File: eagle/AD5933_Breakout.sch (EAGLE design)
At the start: 6 parts, among them U1 AD5933

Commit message: first iteration of board
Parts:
- removed JP3: (no value), SparkFun-Connectors:M04PTH
- added JP1: (no value), SparkFun-Connectors:M04PTH
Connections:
- new net MCLK: JP1.3
- new net SCL: JP1.1
- new net SDA: JP1.2
- new net VCC: JP2.1
- net GND: now also JP1.4
- net RFB: now also JP2.3
- net VIN: now also JP2.2
- net VOUT: now also JP2.4
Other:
- moved on the sheet: JP2
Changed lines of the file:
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@@
 <part name="C2" library="SparkFun-Capacitors" deviceset="0.1UF-100V-10%(0603)" device="" value="10uF"/>
 <part name="GND2" library="SparkFun-Aesthetics" deviceset="GND" device=""/>
+<part name="JP1" library="SparkFun-Connectors" deviceset="M04" device="PTH"/>
 <part name="JP2" library="SparkFun-Connectors" deviceset="M04" device="PTH"/>
-<part name="JP3" library="SparkFun-Connectors" deviceset="M04" device="PTH"/>
 </parts>
 <sheets>
@@
 <instance part="C2" gate="G$1" x="213.36" y="109.22"/>
 <instance part="GND2" gate="1" x="157.48" y="93.98"/>
-<instance part="JP2" gate="G$1" x="93.98" y="96.52"/>
-<instance part="JP3" gate="G$1" x="99.06" y="121.92"/>
+<instance part="JP1" gate="G$1" x="91.44" y="96.52"/>
+<instance part="JP2" gate="G$1" x="96.52" y="121.92"/>
 </instances>
 <busses>
@@
 <wire x1="101.6" y1="93.98" x2="104.14" y2="93.98" width="0.1524" layer="91"/>
 <label x="101.6" y="93.98" size="1.778" layer="95"/>
+<pinref part="JP1" gate="G$1" pin="1"/>
 </segment>
 </net>
@@
 <wire x1="96.52" y1="96.52" x2="104.14" y2="96.52" width="0.1524" layer="91"/>
 <label x="101.6" y="96.52" size="1.778" layer="95"/>
+<pinref part="JP1" gate="G$1" pin="2"/>
 </segment>
 </net>
@@
 <wire x1="96.52" y1="99.06" x2="104.14" y2="99.06" width="0.1524" layer="91"/>
 <label x="101.6" y="99.06" size="1.778" layer="95"/>
+<pinref part="JP1" gate="G$1" pin="3"/>
 </segment>
 </net>
@@
 <wire x1="101.6" y1="121.92" x2="109.22" y2="121.92" width="0.1524" layer="91"/>
 <label x="106.68" y="121.92" size="1.778" layer="95"/>
+<pinref part="JP2" gate="G$1" pin="2"/>
 </segment>
 </net>
@@
 <wire x1="101.6" y1="124.46" x2="109.22" y2="124.46" width="0.1524" layer="91"/>
 <label x="106.68" y="124.46" size="1.778" layer="95"/>
+<pinref part="JP2" gate="G$1" pin="3"/>
 </segment>
 </net>
@@
 <wire x1="101.6" y1="127" x2="109.22" y2="127" width="0.1524" layer="91"/>
 <label x="106.68" y="127" size="1.778" layer="95"/>
+<pinref part="JP2" gate="G$1" pin="4"/>
 </segment>
 </net>
@@
 <wire x1="96.52" y1="101.6" x2="104.14" y2="101.6" width="0.1524" layer="91"/>
 <label x="101.6" y="101.6" size="1.778" layer="95"/>
+<pinref part="JP1" gate="G$1" pin="4"/>
 </segment>
 </net>
@@
 <wire x1="101.6" y1="119.38" x2="109.22" y2="119.38" width="0.1524" layer="91"/>
 <label x="106.68" y="119.38" size="1.778" layer="95"/>
+<pinref part="JP2" gate="G$1" pin="1"/>
 </segment>
 </net>

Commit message: both board and schematic looking good
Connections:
- removed net DVDD: C1.1, C2.1, U1.AVDD1, U1.AVDD2, U1.DVDD
- net MCLK: now also U1.MCLK
- net SCL: now also U1.SCL
- net SDA: now also U1.SDA
- net VCC: now also C1.1, C2.1, U1.AVDD1, U1.AVDD2, U1.DVDD
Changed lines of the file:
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@@
 <part name="FRAME1" library="SparkFun-Aesthetics" deviceset="FRAME-LETTER" device=""/>
 <part name="GND1" library="SparkFun-Aesthetics" deviceset="GND" device=""/>
-<part name="SUPPLY1" library="SparkFun-Aesthetics" deviceset="VCC" device=""/>
+<part name="VCC" library="SparkFun-Aesthetics" deviceset="VCC" device=""/>
 <part name="C1" library="SparkFun-Capacitors" deviceset="0.1UF-100V-10%(0603)" device="" value="0.1uF"/>
 <part name="C2" library="SparkFun-Capacitors" deviceset="0.1UF-100V-10%(0603)" device="" value="10uF"/>
@@
 <instance part="FRAME1" gate="G$2" x="193.04" y="2.54"/>
 <instance part="GND1" gate="1" x="213.36" y="99.06"/>
-<instance part="SUPPLY1" gate="1" x="213.36" y="124.46"/>
+<instance part="VCC" gate="1" x="213.36" y="124.46"/>
 <instance part="C1" gate="G$1" x="203.2" y="109.22"/>
 <instance part="C2" gate="G$1" x="213.36" y="109.22"/>
@@
 <net name="SCL" class="0">
 <segment>
-<wire x1="139.7" y1="124.46" x2="132.08" y2="124.46" width="0.1524" layer="91"/>
-<label x="127" y="124.46" size="1.778" layer="95"/>
-</segment>
-<segment>
 <wire x1="96.52" y1="93.98" x2="99.06" y2="93.98" width="0.1524" layer="91"/>
 <wire x1="99.06" y1="93.98" x2="101.6" y2="93.98" width="0.1524" layer="91"/>
@@
 <pinref part="JP1" gate="G$1" pin="1"/>
 </segment>
+<segment>
+<pinref part="U1" gate="A" pin="SCL"/>
+<wire x1="137.16" y1="124.46" x2="132.08" y2="124.46" width="0.1524" layer="91"/>
+<label x="127" y="124.46" size="1.778" layer="95"/>
+</segment>
 </net>
 <net name="SDA" class="0">
-<segment>
-<wire x1="139.7" y1="121.92" x2="132.08" y2="121.92" width="0.1524" layer="91"/>
-<label x="127" y="121.92" size="1.778" layer="95"/>
-</segment>
 <segment>
 <wire x1="96.52" y1="96.52" x2="104.14" y2="96.52" width="0.1524" layer="91"/>
@@
 <pinref part="JP1" gate="G$1" pin="2"/>
 </segment>
+<segment>
+<pinref part="U1" gate="A" pin="SDA"/>
+<wire x1="137.16" y1="121.92" x2="132.08" y2="121.92" width="0.1524" layer="91"/>
+<label x="127" y="121.92" size="1.778" layer="95"/>
+</segment>
 </net>
 <net name="MCLK" class="0">
-<segment>
-<wire x1="139.7" y1="119.38" x2="132.08" y2="119.38" width="0.1524" layer="91"/>
-<label x="127" y="119.38" size="1.778" layer="95"/>
-</segment>
 <segment>
 <wire x1="96.52" y1="99.06" x2="104.14" y2="99.06" width="0.1524" layer="91"/>
 <label x="101.6" y="99.06" size="1.778" layer="95"/>
 <pinref part="JP1" gate="G$1" pin="3"/>
+</segment>
+<segment>
+<pinref part="U1" gate="A" pin="MCLK"/>
+<wire x1="137.16" y1="119.38" x2="132.08" y2="119.38" width="0.1524" layer="91"/>
+<label x="127" y="119.38" size="1.778" layer="95"/>
 </segment>
 </net>
@@
 </segment>
 </net>
-<net name="DVDD" class="0">
+<net name="VCC" class="0">
+<segment>
+<wire x1="101.6" y1="119.38" x2="109.22" y2="119.38" width="0.1524" layer="91"/>
+<label x="106.68" y="119.38" size="1.778" layer="95"/>
+<pinref part="JP2" gate="G$1" pin="1"/>
+</segment>
 <segment>
 <pinref part="U1" gate="A" pin="DVDD"/>
@@
 </segment>
 <segment>
+<pinref part="U1" gate="A" pin="AVDD1"/>
+<wire x1="185.42" y1="119.38" x2="177.8" y2="119.38" width="0.1524" layer="91"/>
+<wire x1="185.42" y1="116.84" x2="185.42" y2="119.38" width="0.1524" layer="91"/>
+<pinref part="U1" gate="A" pin="AVDD2"/>
+<wire x1="177.8" y1="116.84" x2="185.42" y2="116.84" width="0.1524" layer="91"/>
+<label x="180.34" y="119.38" size="1.778" layer="95"/>
+</segment>
+<segment>
 <wire x1="203.2" y1="114.3" x2="203.2" y2="119.38" width="0.1524" layer="91"/>
 <wire x1="203.2" y1="119.38" x2="213.36" y2="119.38" width="0.1524" layer="91"/>
 <wire x1="213.36" y1="119.38" x2="213.36" y2="114.3" width="0.1524" layer="91"/>
-<pinref part="SUPPLY1" gate="1" pin="VCC"/>
+<pinref part="VCC" gate="1" pin="VCC"/>
 <wire x1="213.36" y1="124.46" x2="213.36" y2="119.38" width="0.1524" layer="91"/>
 <junction x="213.36" y="119.38"/>
-<pinref part="U1" gate="A" pin="AVDD2"/>
-<wire x1="177.8" y1="116.84" x2="185.42" y2="116.84" width="0.1524" layer="91"/>
-<wire x1="185.42" y1="116.84" x2="185.42" y2="119.38" width="0.1524" layer="91"/>
-<pinref part="U1" gate="A" pin="AVDD1"/>
-<wire x1="185.42" y1="119.38" x2="177.8" y2="119.38" width="0.1524" layer="91"/>
-<wire x1="185.42" y1="119.38" x2="203.2" y2="119.38" width="0.1524" layer="91"/>
-<junction x="185.42" y="119.38"/>
-<junction x="203.2" y="119.38"/>
-<wire x1="177.8" y1="114.3" x2="185.42" y2="114.3" width="0.1524" layer="91"/>
-<label x="180.34" y="114.3" size="1.778" layer="95"/>
-<wire x1="185.42" y1="116.84" x2="185.42" y2="114.3" width="0.1524" layer="91"/>
-<junction x="185.42" y="116.84"/>
 <pinref part="C1" gate="G$1" pin="1"/>
 <pinref part="C2" gate="G$1" pin="1"/>
 </segment>
 </net>
-<net name="VCC" class="0">
-<segment>
-<wire x1="101.6" y1="119.38" x2="109.22" y2="119.38" width="0.1524" layer="91"/>
-<label x="106.68" y="119.38" size="1.778" layer="95"/>
-<pinref part="JP2" gate="G$1" pin="1"/>
-</segment>
-</net>

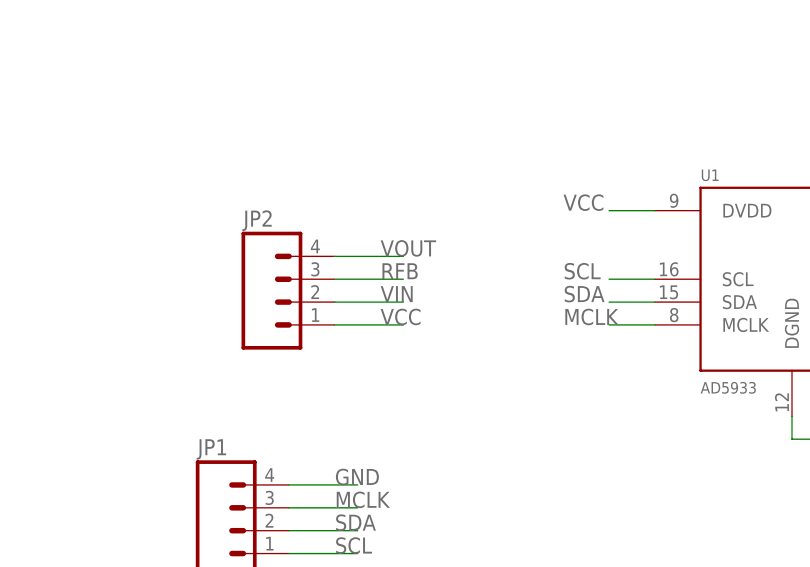
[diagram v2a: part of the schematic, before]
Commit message: switched headers and rerouted all pins
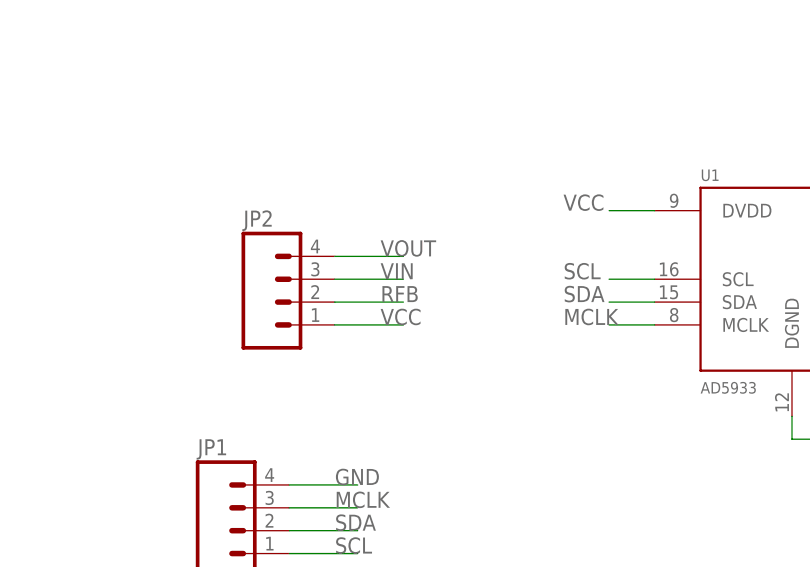
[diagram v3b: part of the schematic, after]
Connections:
- net RFB: now also JP2.2; no longer JP2.3
- net VIN: now also JP2.3; no longer JP2.2
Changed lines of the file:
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@@
 </segment>
 <segment>
-<wire x1="101.6" y1="121.92" x2="109.22" y2="121.92" width="0.1524" layer="91"/>
-<label x="106.68" y="121.92" size="1.778" layer="95"/>
-<pinref part="JP2" gate="G$1" pin="2"/>
+<wire x1="101.6" y1="124.46" x2="109.22" y2="124.46" width="0.1524" layer="91"/>
+<label x="106.68" y="124.46" size="1.778" layer="95"/>
+<pinref part="JP2" gate="G$1" pin="3"/>
 </segment>
 </net>
@@
 </segment>
 <segment>
-<wire x1="101.6" y1="124.46" x2="109.22" y2="124.46" width="0.1524" layer="91"/>
-<label x="106.68" y="124.46" size="1.778" layer="95"/>
-<pinref part="JP2" gate="G$1" pin="3"/>
+<wire x1="101.6" y1="121.92" x2="109.22" y2="121.92" width="0.1524" layer="91"/>
+<label x="106.68" y="121.92" size="1.778" layer="95"/>
+<pinref part="JP2" gate="G$1" pin="2"/>
 </segment>
 </net>

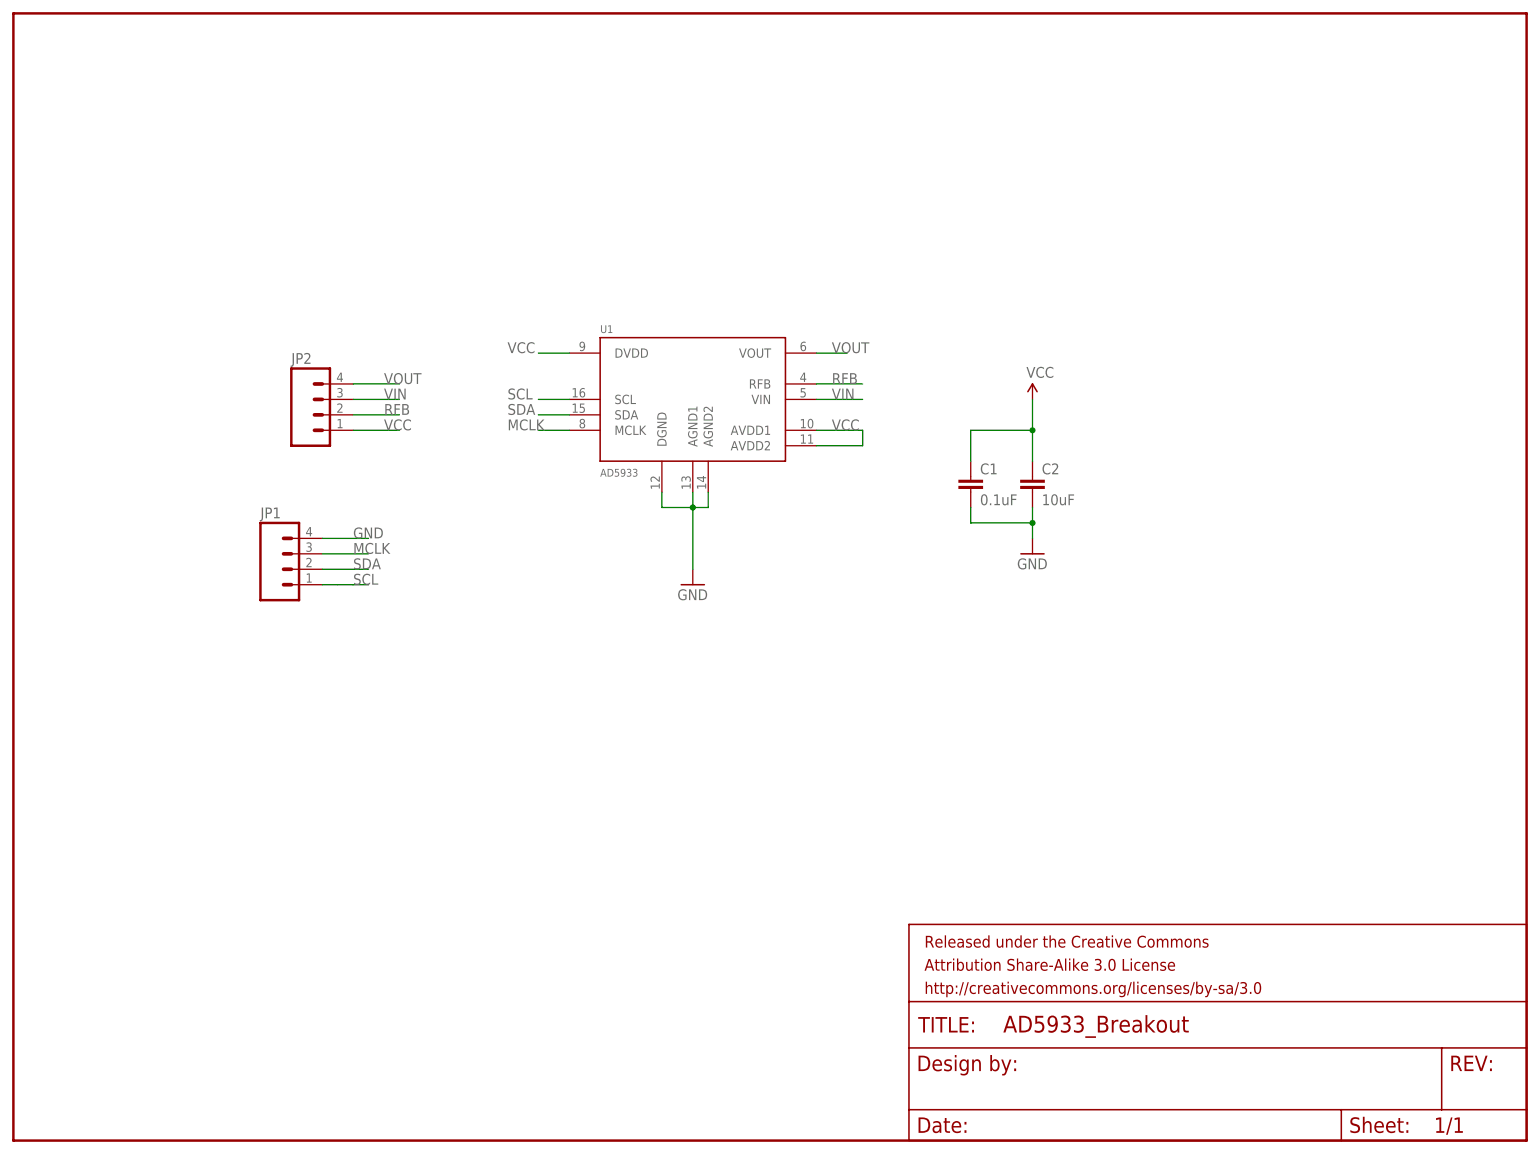
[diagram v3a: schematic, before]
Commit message: fixed rules and cleared clearance errors
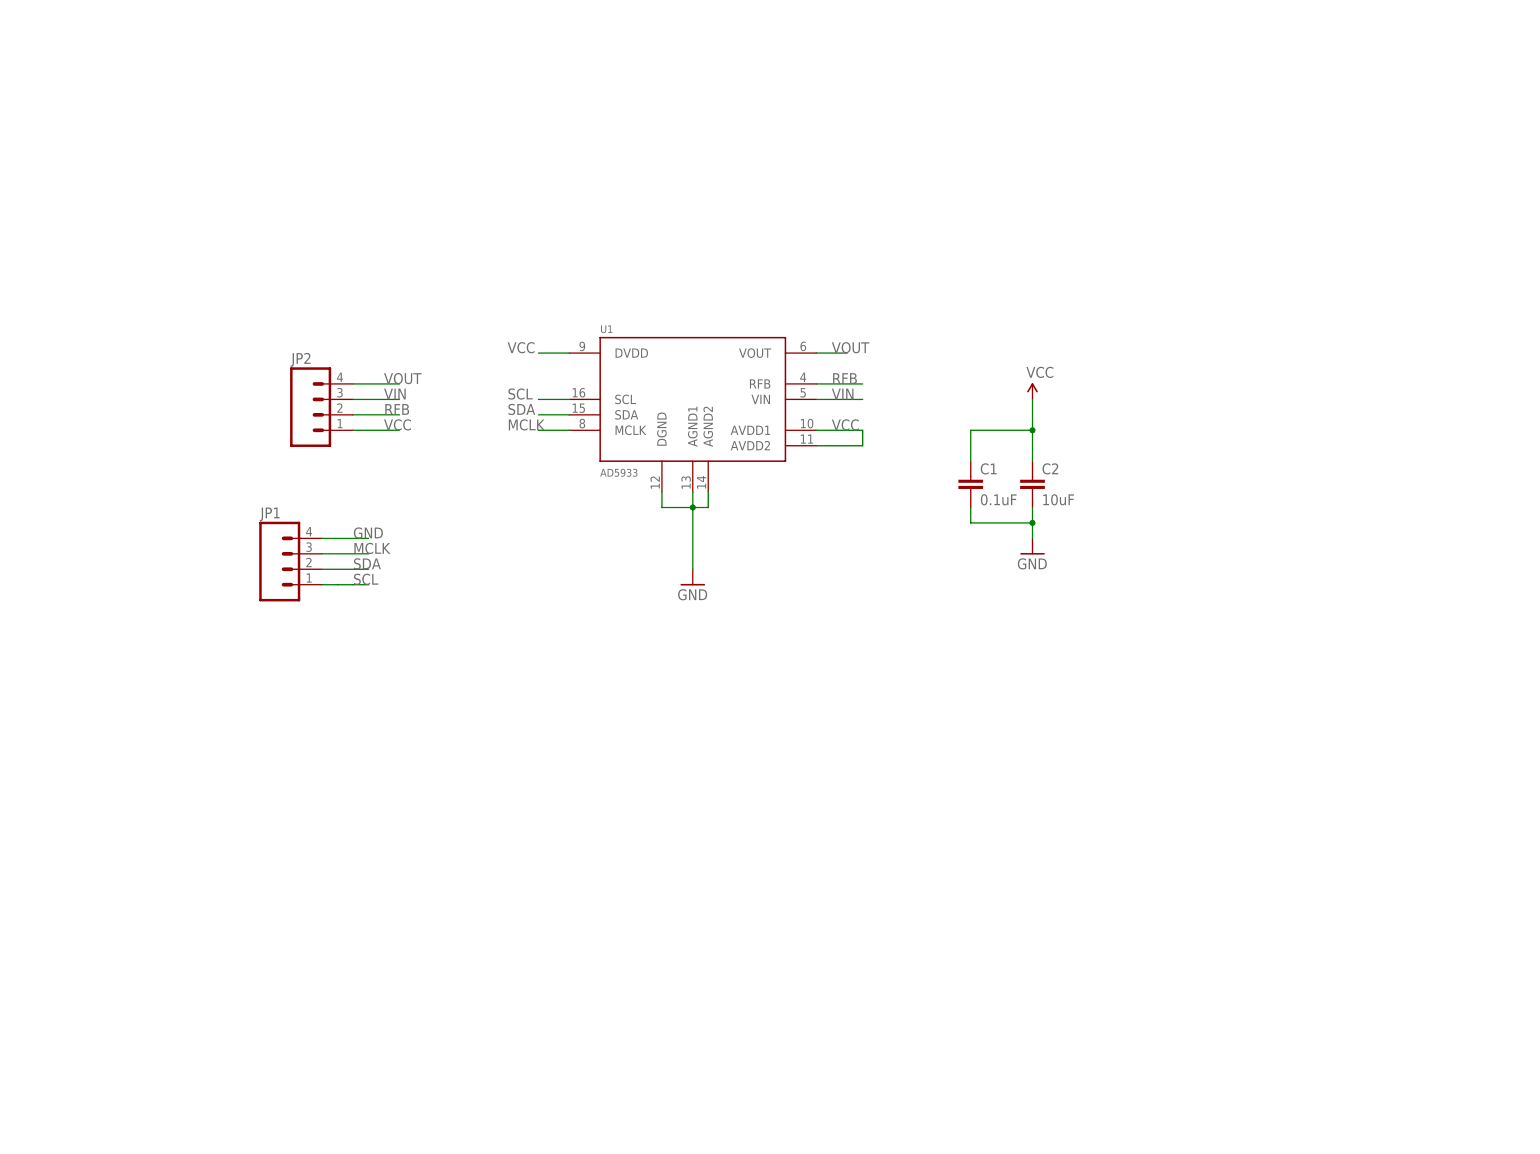
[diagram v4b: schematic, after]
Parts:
- removed FRAME1: FRAME-LETTER, SparkFun-Aesthetics:FRAME-LETTER
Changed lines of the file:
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@@
 <?xml version="1.0" encoding="utf-8"?>
 <!DOCTYPE eagle SYSTEM "eagle.dtd">
-<eagle version="6.5.0">
+<eagle version="6.4">
 <drawing>
 <settings>
@@
 <parts>
 <part name="U1" library="kblom" deviceset="AD5933" device=""/>
-<part name="FRAME1" library="SparkFun-Aesthetics" deviceset="FRAME-LETTER" device=""/>
 <part name="GND1" library="SparkFun-Aesthetics" deviceset="GND" device=""/>
 <part name="VCC" library="SparkFun-Aesthetics" deviceset="VCC" device=""/>
@@
 <instances>
 <instance part="U1" gate="A" x="157.48" y="124.46"/>
-<instance part="FRAME1" gate="G$1" x="45.72" y="2.54"/>
-<instance part="FRAME1" gate="G$2" x="193.04" y="2.54"/>
 <instance part="GND1" gate="1" x="213.36" y="99.06"/>
 <instance part="VCC" gate="1" x="213.36" y="124.46"/>
